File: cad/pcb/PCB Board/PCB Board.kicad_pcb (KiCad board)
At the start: 2 copper layers, 86 x 86 mm, 70 parts, among them J1 USB4105, J2 S2B-PH-K-S, Q1 FDN340P, Q2 BSS138, Q3 MMFTN170, SW1 PTS645, SW2 PTS645, SW3 PTS645, SW4 PTS645, SW5 PTS645, SW6 PTS645, SW7 SLW-1277545-3A-RA-N-D, U1 ESP32-C3-WROOM-02, U2 TLV75533PDYDR, U3 TP4057

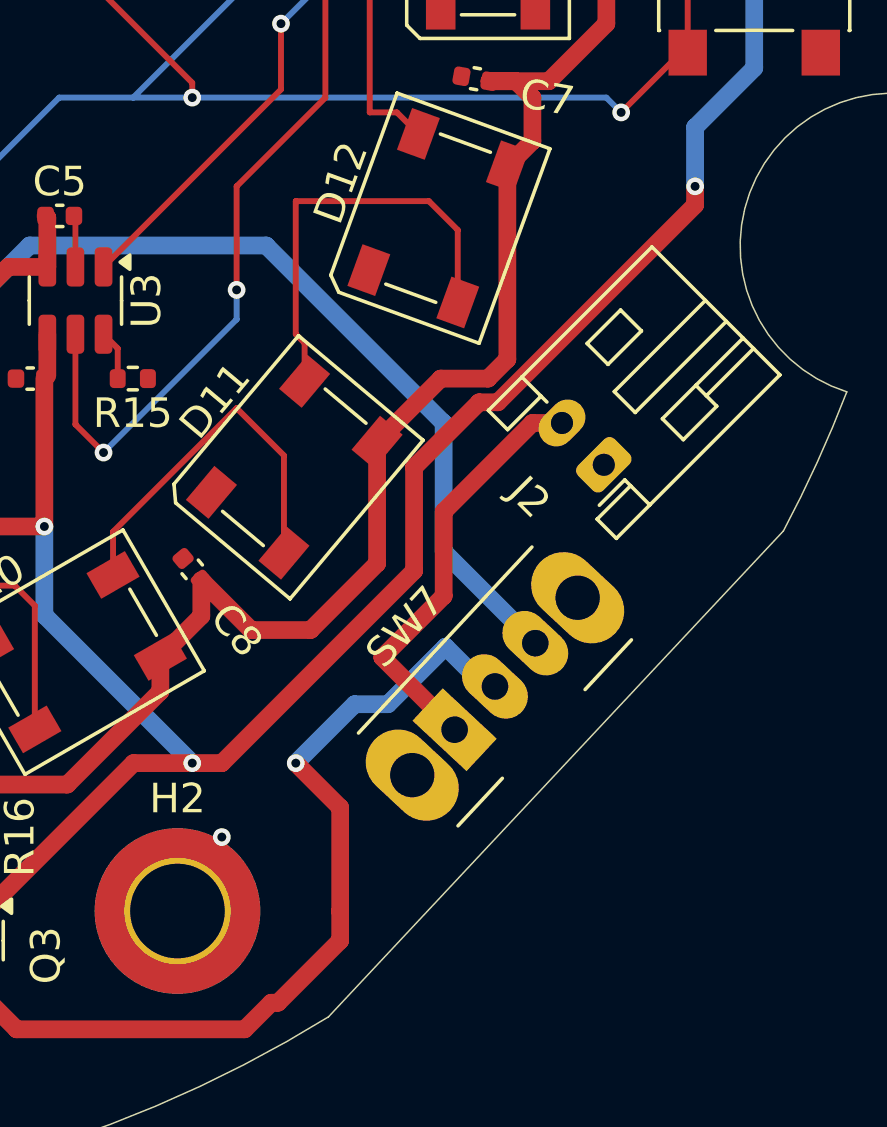
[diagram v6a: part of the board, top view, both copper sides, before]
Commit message: fixed a wrong switch footprint
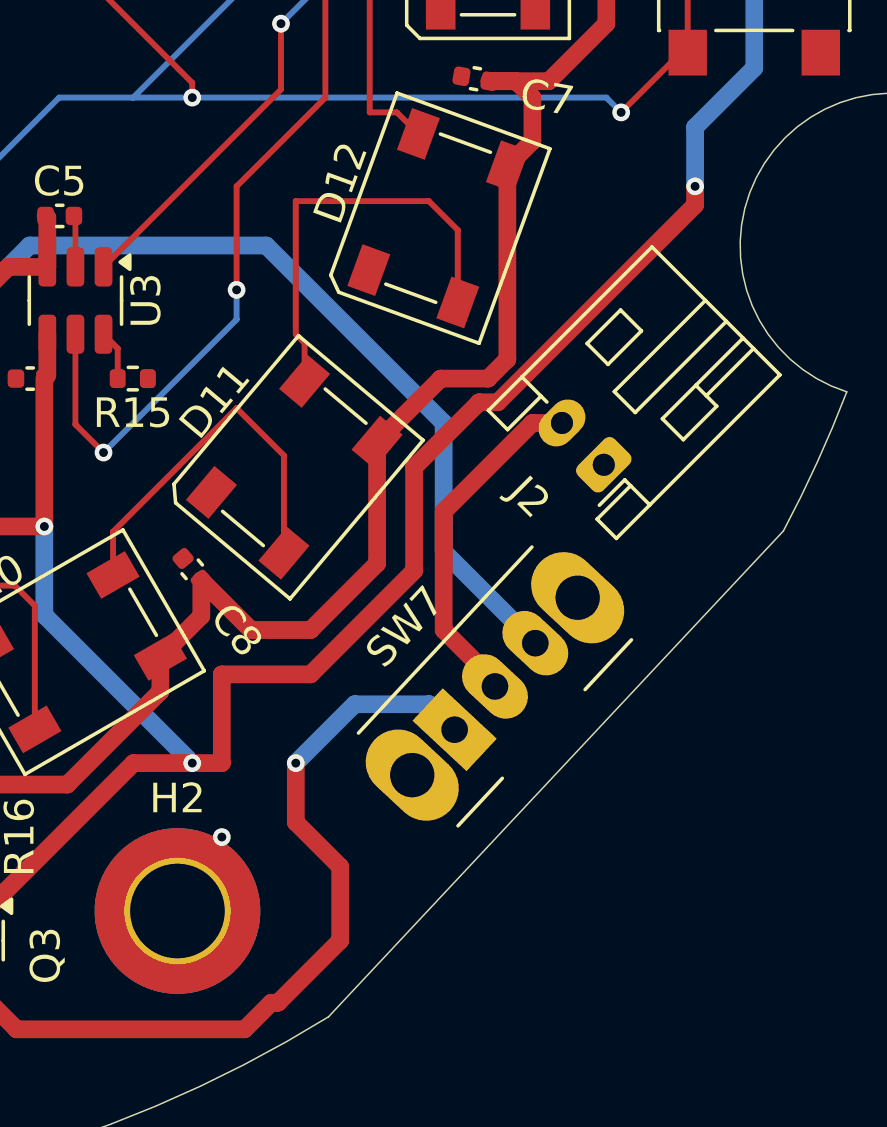
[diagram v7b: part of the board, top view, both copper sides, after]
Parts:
- Q3: value MMFTN170 -> NDS331N
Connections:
- SW7 pad 1: Net-(J2-Pin_2) -> Net-(Q3-D)
- SW7 pad 2: Net-(Q3-D) -> Net-(J2-Pin_2)
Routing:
- net Net-(Q3-D): track 31.4 -> 28.3 mm
- net VBUS: track 143.8 -> 145.5 mm
- net Net-(J2-Pin_2): track 14.5 -> 13.0 mm
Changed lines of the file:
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@@
 			)
 		)
-		(property "Datasheet" "https://www.we-https://www.mouser.de/datasheet/2/1628/slw_1277545_3a_ra_n_d-3510939.pdf"
+		(property "Datasheet" "https://www.lcsc.com/datasheet/lcsc_datasheet_1912111437_SHOU-HAN-SK12D07VG3_C431547.pdf"
 			(at 0 0 47)
 			(unlocked yes)
@@
 			)
 		)
+		(property "LCSC" "C431547"
+			(at 0 0 47)
+			(unlocked yes)
+			(layer "F.Fab")
+			(hide yes)
+			(effects
+				(font
+					(size 1 1)
+					(thickness 0.15)
+				)
+			)
+		)
 		(property ki_fp_filters "SW*Wuerth*WS*SLTV*10x2.5x6.4*P2.54mm*")
 		(sheetname "/")
@@
 			(layers "*.Cu" "*.Mask")
 			(remove_unused_layers no)
-			(net 40 "Net-(J2-Pin_2)")
-			(pinfunction "B")
+			(net 42 "Net-(Q3-D)")
+			(pinfunction "C")
 			(pintype "passive")
 		)
@@
 			(layers "*.Cu" "*.Mask")
 			(remove_unused_layers no)
-			(net 42 "Net-(Q3-D)")
-			(pinfunction "C")
+			(net 40 "Net-(J2-Pin_2)")
+			(pinfunction "B")
 			(pintype "passive")
 		)
@@
 			)
 		)
-		(property "Value" "MMFTN170"
+		(property "Value" "NDS331N"
 			(at 0 2.4 90)
 			(layer "F.Fab")
@@
 			)
 		)
-		(property "Datasheet" "https://diotec.com/request/datasheet/mmftn170.pdf"
+		(property "Datasheet" "https://www.onsemi.com/download/data-sheet/pdf/nds331n-d.pdf"
 			(at 0 0 90)
 			(layer "F.Fab")
@@
 			)
 		)
-		(property "Description" "50V Vds, 0.5A Id, N-Channel MOSFET, SOT-23"
+		(property "Description" "20V Vds, 0.5A Id, N-Channel MOSFET, SOT-23"
 			(at 0 0 90)
 			(layer "F.Fab")
@@
 	)
 	(segment
-		(start 92.299 79.701)
-		(end 90.1 81.9)
+		(start 90.1 81.9)
+		(end 92.299 79.701)
 		(width 0.6)
 		(layer "F.Cu")
@@
 	)
 	(segment
+		(start 83.6 91.9)
+		(end 83.6 88.9)
+		(width 0.6)
+		(layer "F.Cu")
+		(net 5)
+	)
+	(segment
 		(start 75.6 96.9625)
 		(end 75.6 94.91)
@@
 	)
 	(segment
+		(start 90.1 85.4)
+		(end 90.1 81.9)
+		(width 0.6)
+		(layer "F.Cu")
+		(net 5)
+	)
+	(segment
 		(start 72.6 83.9)
 		(end 77.6 83.9)
@@
 	)
 	(segment
-		(start 90.1 81.9)
+		(start 89.494112 42.9)
+		(end 88.732786 42.9)
+		(width 0.6)
+		(layer "F.Cu")
+		(net 5)
+	)
+	(segment
+		(start 86.6 88.9)
 		(end 90.1 85.4)
 		(width 0.6)
@@
 	)
 	(segment
-		(start 89.494112 42.9)
-		(end 88.732786 42.9)
+		(start 92.931785 79.701)
+		(end 99.6 73.032785)
 		(width 0.6)
 		(layer "F.Cu")
@@
 	)
 	(segment
+		(start 92.299 79.701)
+		(end 92.931785 79.701)
+		(width 0.6)
+		(layer "F.Cu")
+		(net 5)
+	)
+	(segment
 		(start 95.1 46.4)
 		(end 90.6 41.9)
@@
 	)
 	(segment
-		(start 99.6 72.4)
-		(end 99.6 73.032785)
-		(width 0.6)
-		(layer "F.Cu")
-		(net 5)
-	)
-	(segment
 		(start 83.901 38.731786)
 		(end 83.901 38.099)
@@
 	)
 	(segment
-		(start 90.1 85.4)
-		(end 83.6 91.9)
+		(start 83.6 88.9)
+		(end 86.6 88.9)
 		(width 0.6)
 		(layer "F.Cu")
@@
 	)
 	(segment
-		(start 83.6 91.9)
-		(end 82.6 91.9)
-		(width 0.6)
-		(layer "F.Cu")
-		(net 5)
-	)
-	(segment
 		(start 65.6 77.9)
 		(end 68.1 77.9)
@@
 	)
 	(segment
+		(start 82.6 91.9)
+		(end 83.6 91.9)
+		(width 0.6)
+		(layer "F.Cu")
+		(net 5)
+	)
+	(segment
 		(start 75.6 96.9625)
 		(end 75.55 96.9625)
@@
 	)
 	(segment
-		(start 99.6 73.032785)
-		(end 92.931785 79.701)
-		(width 0.6)
-		(layer "F.Cu")
-		(net 5)
-	)
-	(segment
-		(start 92.931785 79.701)
-		(end 92.299 79.701)
+		(start 85.799751 41.599751)
+		(end 83.901 39.701)
 		(width 0.6)
 		(layer "F.Cu")
@@
 	)
 	(segment
-		(start 85.799751 41.599751)
-		(end 83.901 39.701)
+		(start 87.364892 42.195678)
+		(end 86.404467 42.195678)
 		(width 0.6)
 		(layer "F.Cu")
@@
 	)
 	(segment
-		(start 87.364892 42.195678)
-		(end 86.404467 42.195678)
+		(start 99.6 73.032785)
+		(end 99.6 72.4)
 		(width 0.6)
 		(layer "F.Cu")
@@
 	)
 	(segment
-		(start 95.1 80.4)
-		(end 94.1 80.4)
+		(start 91.1 83.4)
+		(end 91.1 87.4)
 		(width 0.6)
 		(layer "F.Cu")
@@
 	)
 	(segment
-		(start 91.1 83.4)
-		(end 91.1 86.249942)
+		(start 92.834054 89.134054)
+		(end 92.834054 89.307349)
 		(width 0.6)
 		(layer "F.Cu")
@@
 	)
 	(segment
-		(start 89.024971 88.324971)
-		(end 91.470058 90.770058)
+		(start 95.1 80.4)
+		(end 94.1 80.4)
+		(width 0.6)
+		(layer "F.Cu")
+		(net 40)
+	)
+	(segment
+		(start 93.396749 89.870044)
+		(end 92.834054 89.307349)
 		(width 0.6)
 		(layer "F.Cu")
@@
 	)
 	(segment
-		(start 91.1 86.249942)
-		(end 89.024971 88.324971)
+		(start 91.1 87.4)
+		(end 92.834054 89.134054)
 		(width 0.6)
 		(layer "F.Cu")
@@
 	)
 	(segment
+		(start 92.507349 89.307349)
+		(end 92.834054 89.307349)
+		(width 0.6)
+		(layer "B.Cu")
+		(net 40)
+	)
+	(segment
 		(start 45.1 68.4)
 		(end 47.09 68.4)
@@
 	)
 	(segment
-		(start 87.6 93.4)
-		(end 86.1 91.9)
-		(width 0.6)
-		(layer "F.Cu")
-		(net 42)
-	)
-	(segment
-		(start 76.6625 100.9)
-		(end 84.371189 100.9)
+		(start 74.6 98.8375)
+		(end 76.6625 100.9)
 		(width 0.6)
 		(layer "F.Cu")
@@
 	)
 	(segment
-		(start 74.6 98.8375)
-		(end 76.6625 100.9)
+		(start 86.1 93.9)
+		(end 86.1 91.9)
 		(width 0.6)
 		(layer "F.Cu")
@@
 	)
 	(segment
-		(start 93.396749 89.870044)
-		(end 92.834054 89.307349)
+		(start 85.499472 100.001)
+		(end 87.6 97.900472)
 		(width 0.6)
 		(layer "F.Cu")
@@
 	)
 	(segment
-		(start 87.6 96.9)
-		(end 87.6 93.4)
+		(start 84.371189 100.9)
+		(end 85.270188 100.001)
 		(width 0.6)
 		(layer "F.Cu")
@@
 	(segment
 		(start 87.6 97.900472)
-		(end 87.6 96.9)
+		(end 87.6 95.4)
 		(width 0.6)
 		(layer "F.Cu")
@@
 	)
 	(segment
-		(start 84.371189 100.9)
-		(end 85.270188 100.001)
+		(start 76.6625 100.9)
+		(end 84.371189 100.9)
 		(width 0.6)
 		(layer "F.Cu")
@@
 	)
 	(segment
-		(start 85.499472 100.001)
-		(end 87.6 97.900472)
+		(start 87.6 95.4)
+		(end 86.1 93.9)
 		(width 0.6)
 		(layer "F.Cu")
@@
 	(segment
 		(start 88.091331 89.908669)
-		(end 89.217593 89.908669)
-		(width 0.6)
-		(layer "B.Cu")
-		(net 42)
-	)
-	(segment
-		(start 86.1 91.9)
-		(end 88.091331 89.908669)
+		(end 90.608669 89.908669)
 		(width 0.6)
 		(layer "B.Cu")
@@
 	)
 	(segment
-		(start 92.507349 89.307349)
-		(end 92.834054 89.307349)
-		(width 0.6)
-		(layer "B.Cu")
-		(net 42)
-	)
-	(segment
-		(start 89.217593 89.908669)
-		(end 91.163131 87.963131)
+		(start 90.608669 89.908669)
+		(end 91.470058 90.770058)
 		(width 0.6)
 		(layer "B.Cu")
@@
 	)
 	(segment
-		(start 91.163131 87.963131)
-		(end 92.507349 89.307349)
+		(start 86.1 91.9)
+		(end 88.091331 89.908669)
 		(width 0.6)
 		(layer "B.Cu")
